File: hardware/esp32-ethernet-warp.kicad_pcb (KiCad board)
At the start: 4 copper layers, 104 x 42 mm, 117 parts, among them J201 TJLC_001LA1, P101 FLASH, P201 CON-SENSOR2, P202 CON-SENSOR2, P205 CON-SENSOR2, P206 CON-SENSOR2, Q101 BC817, Q102 BC817, SW101 B3U-1000P, SW102 B3U-1000P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

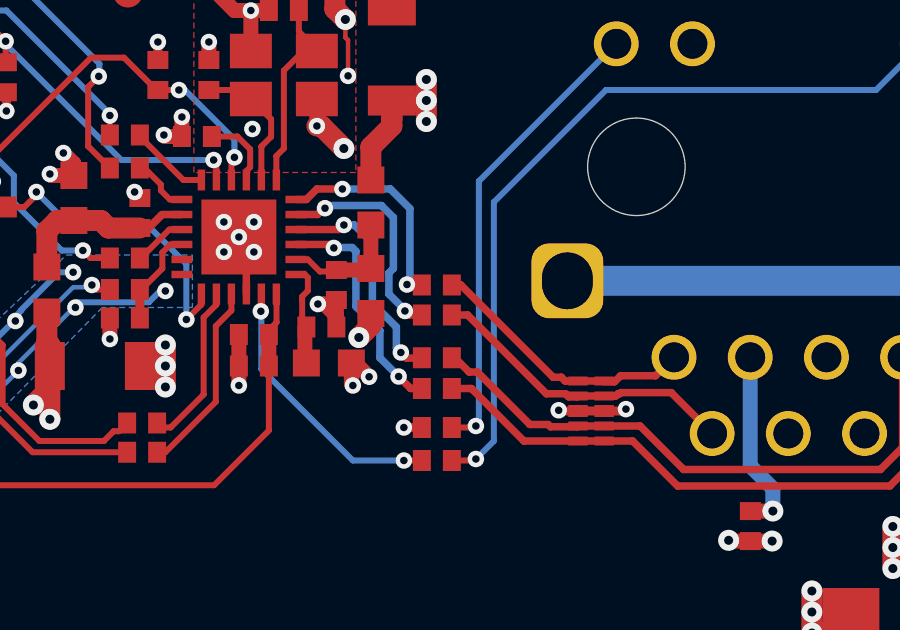
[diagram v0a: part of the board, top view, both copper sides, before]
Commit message: Revert "fix ethernet bug"
This reverts commit b0ba0365b1ecd3ee5b273f32dcba04a8b2befd97.
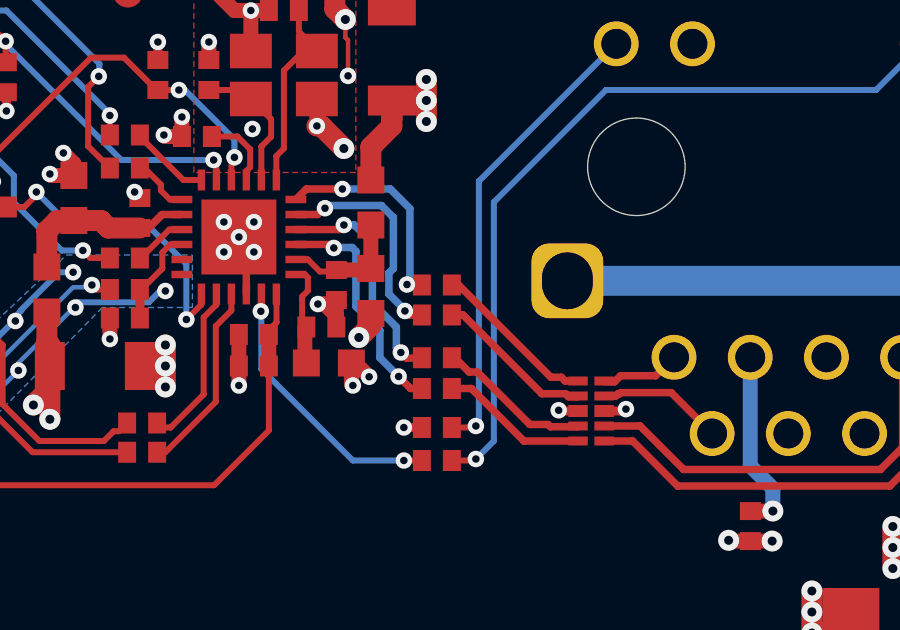
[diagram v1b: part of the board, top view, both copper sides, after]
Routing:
- net TXOPx: track 9.20 -> 8.22 mm
- net RXIPx: track 19.9 -> 19.0 mm
- net TXONx: track 10.4 -> 9.53 mm
- net RXINx: track 18.8 -> 17.9 mm
- net GND: track 266.9 -> 266.1 mm
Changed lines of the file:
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@@
   (segment (start 173.675 54.1) (end 174.375 54.1) (width 0.7) (layer "F.Cu") (net 1))
   (segment (start 201.45 26.635) (end 202.15 26.635) (width 0.5) (layer "F.Cu") (net 1))
-  (segment (start 240.755 32.25) (end 241.6 32.25) (width 0.3) (layer "F.Cu") (net 1))
   (segment (start 183.2233 40.7267) (end 183.225 40.725) (width 0.3) (layer "F.Cu") (net 1))
   (segment (start 229.85018 20.2499) (end 229.85018 18.90018) (width 0.5) (layer "F.Cu") (net 1))
@@
   (segment (start 221.675 20.025) (end 221.675 19.925) (width 0.2) (layer "B.Cu") (net 85))
   (segment (start 225.534166 23.884166) (end 221.675 20.025) (width 0.2) (layer "B.Cu") (net 85))
-  (segment (start 232.05 24.85) (end 232.9 24.85) (width 0.25) (layer "F.Cu") (net 86))
-  (segment (start 231.34992 25.20032) (end 231.69968 25.20032) (width 0.25) (layer "F.Cu") (net 86))
-  (segment (start 231.69968 25.20032) (end 232.05 24.85) (width 0.25) (layer "F.Cu") (net 86))
+  (segment (start 231.34992 25.20032) (end 231.70024 24.85) (width 0.25) (layer "F.Cu") (net 86))
+  (segment (start 231.70024 24.85) (end 232.9 24.85) (width 0.25) (layer "F.Cu") (net 86))
   (segment (start 235.069239 28.05) (end 235.053503 28.034264) (width 0.25) (layer "F.Cu") (net 86))
   (segment (start 235.55 28.05) (end 235.069239 28.05) (width 0.25) (layer "F.Cu") (net 86))
@@
   (segment (start 169.325 49.05) (end 167.725 49.05) (width 0.5) (layer "F.Cu") (net 138))
   (segment (start 168.025 49.15) (end 167.725 49.15) (width 0.2) (layer "F.Cu") (net 138))
-  (segment (start 236.85 28.05) (end 236.55 28.05) (width 0.25) (layer "F.Cu") (net 139))
-  (segment (start 239.925 31.125) (end 236.85 28.05) (width 0.25) (layer "F.Cu") (net 139))
+  (segment (start 239.85 31.125) (end 236.775 28.05) (width 0.25) (layer "F.Cu") (net 139))
   (segment (start 240.325 31.25) (end 240.2 31.125) (width 0.25) (layer "F.Cu") (net 139))
-  (segment (start 240.2 31.125) (end 239.925 31.125) (width 0.25) (layer "F.Cu") (net 139))
-  (segment (start 241.625 31.25) (end 240.65 31.25) (width 0.25) (layer "F.Cu") (net 139))
+  (segment (start 240.2 31.125) (end 239.85 31.125) (width 0.25) (layer "F.Cu") (net 139))
+  (segment (start 236.775 28.05) (end 236.55 28.05) (width 0.25) (layer "F.Cu") (net 139))
   (segment (start 243.34 31.075) (end 243.955 30.46) (width 0.25) (layer "F.Cu") (net 139))
   (segment (start 240.755 31.25) (end 240.325 31.25) (width 0.25) (layer "F.Cu") (net 139))
@@
   (segment (start 241.6 31.275) (end 241.975 31.275) (width 0.25) (layer "F.Cu") (net 139))
   (segment (start 242.175 31.075) (end 243.34 31.075) (width 0.25) (layer "F.Cu") (net 139))
+  (segment (start 240.755 31.75) (end 240.73 31.775) (width 0.25) (layer "F.Cu") (net 140))
+  (segment (start 236.925 29.05) (end 236.55 29.05) (width 0.25) (layer "F.Cu") (net 140))
   (segment (start 242.08608 31.675) (end 242.01108 31.75) (width 0.25) (layer "F.Cu") (net 140))
+  (segment (start 245.225 33) (end 243.862423 31.637423) (width 0.25) (layer "F.Cu") (net 140))
+  (segment (start 243.862423 31.637423) (end 242.178263 31.637423) (width 0.25) (layer "F.Cu") (net 140))
+  (segment (start 240.73 31.775) (end 240.437534 31.775) (width 0.25) (layer "F.Cu") (net 140))
   (segment (start 240.437534 31.775) (end 240.337534 31.675) (width 0.25) (layer "F.Cu") (net 140))
-  (segment (start 245.225 33) (end 243.862423 31.637423) (width 0.25) (layer "F.Cu") (net 140))
-  (segment (start 240.337534 31.675) (end 239.7 31.675) (width 0.25) (layer "F.Cu") (net 140))
-  (segment (start 243.862423 31.637423) (end 242.178263 31.637423) (width 0.25) (layer "F.Cu") (net 140))
-  (segment (start 239.7 31.675) (end 237.075 29.05) (width 0.25) (layer "F.Cu") (net 140))
   (segment (start 242.01108 31.75) (end 241.65 31.75) (width 0.25) (layer "F.Cu") (net 140))
-  (segment (start 240.73 31.775) (end 240.437534 31.775) (width 0.25) (layer "F.Cu") (net 140))
-  (segment (start 241.625 31.75) (end 240.75 31.75) (width 0.25) (layer "F.Cu") (net 140))
-  (segment (start 240.755 31.75) (end 240.73 31.775) (width 0.25) (layer "F.Cu") (net 140))
   (segment (start 242.178263 31.637423) (end 242.140685 31.675) (width 0.25) (layer "F.Cu") (net 140))
   (segment (start 242.140685 31.675) (end 242.08608 31.675) (width 0.25) (layer "F.Cu") (net 140))
-  (segment (start 237.075 29.05) (end 236.55 29.05) (width 0.25) (layer "F.Cu") (net 140))
-  (segment (start 239.832398 32.7755) (end 239.756898 32.7) (width 0.25) (layer "F.Cu") (net 141))
+  (segment (start 240.337534 31.675) (end 239.55 31.675) (width 0.25) (layer "F.Cu") (net 140))
+  (segment (start 239.55 31.675) (end 236.925 29.05) (width 0.25) (layer "F.Cu") (net 140))
   (segment (start 241.625 32.75) (end 242.825 32.75) (width 0.25) (layer "F.Cu") (net 141))
   (segment (start 240.7295 32.7755) (end 239.832398 32.7755) (width 0.25) (layer "F.Cu") (net 141))
   (segment (start 237.4 30.95) (end 237.125 30.95) (width 0.25) (layer "F.Cu") (net 141))
+  (segment (start 237.125 30.95) (end 236.675 30.5) (width 0.25) (layer "F.Cu") (net 141))
   (segment (start 242.825 32.75) (end 244.275 34.2) (width 0.25) (layer "F.Cu") (net 141))
   (segment (start 236.675 30.5) (end 236.55 30.5) (width 0.25) (layer "F.Cu") (net 141))
+  (segment (start 251.575 33.46) (end 251.575 30.46) (width 0.25) (layer "F.Cu") (net 141))
+  (segment (start 250.835 34.2) (end 251.575 33.46) (width 0.25) (layer "F.Cu") (net 141))
+  (segment (start 244.275 34.2) (end 250.835 34.2) (width 0.25) (layer "F.Cu") (net 141))
+  (segment (start 239.15 32.7) (end 237.4 30.95) (width 0.25) (layer "F.Cu") (net 141))
+  (segment (start 239.756898 32.7) (end 239.15 32.7) (width 0.25) (layer "F.Cu") (net 141))
   (segment (start 240.755 32.75) (end 240.7295 32.7755) (width 0.25) (layer "F.Cu") (net 141))
-  (segment (start 241.625 32.75) (end 240.7 32.75) (width 0.25) (layer "F.Cu") (net 141))
-  (segment (start 251.575 33.46) (end 251.575 30.46) (width 0.25) (layer "F.Cu") (net 141))
-  (segment (start 237.125 30.95) (end 236.675 30.5) (width 0.25) (layer "F.Cu") (net 141))
-  (segment (start 250.835 34.2) (end 251.575 33.46) (width 0.25) (layer "F.Cu") (net 141))
-  (segment (start 239.15 32.7) (end 237.4 30.95) (width 0.25) (layer "F.Cu") (net 141))
-  (segment (start 244.275 34.2) (end 250.835 34.2) (width 0.25) (layer "F.Cu") (net 141))
-  (segment (start 239.756898 32.7) (end 239.15 32.7) (width 0.25) (layer "F.Cu") (net 141))
-  (segment (start 241.625 33.25) (end 240.75 33.25) (width 0.25) (layer "F.Cu") (net 142))
+  (segment (start 239.832398 32.7755) (end 239.756898 32.7) (width 0.25) (layer "F.Cu") (net 141))
   (segment (start 241.625 33.25) (end 242.575 33.25) (width 0.25) (layer "F.Cu") (net 142))
   (segment (start 252.6 33.85) (end 252.85 33.6) (width 0.25) (layer "F.Cu") (net 142))

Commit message: fix ethernet bug
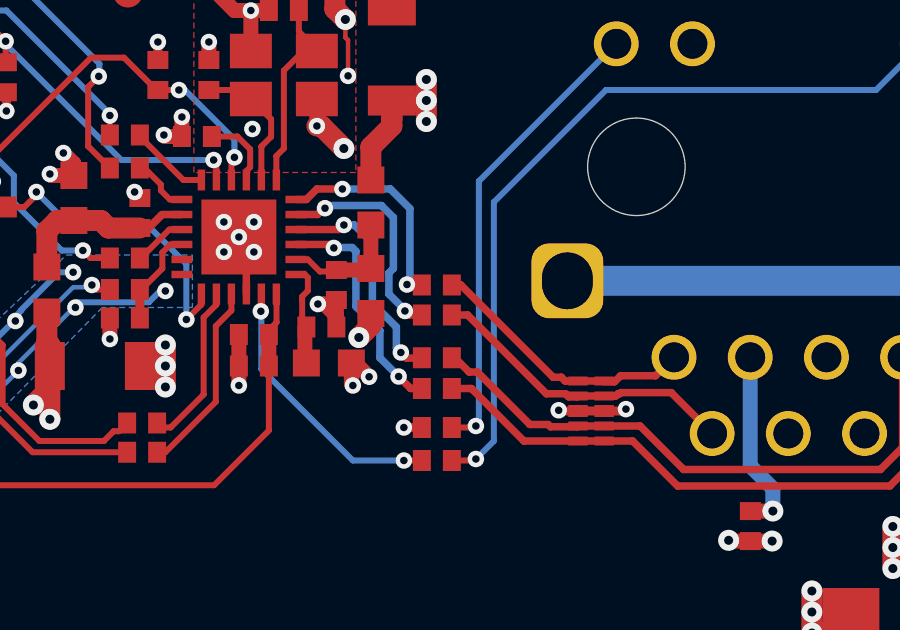
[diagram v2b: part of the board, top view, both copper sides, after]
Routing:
- net TXOPx: track 8.22 -> 9.20 mm
- net RXIPx: track 19.0 -> 19.9 mm
- net TXONx: track 9.53 -> 10.4 mm
- net RXINx: track 17.9 -> 18.8 mm
- net GND: track 266.1 -> 266.9 mm
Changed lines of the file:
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@@
   (segment (start 173.675 54.1) (end 174.375 54.1) (width 0.7) (layer "F.Cu") (net 1))
   (segment (start 201.45 26.635) (end 202.15 26.635) (width 0.5) (layer "F.Cu") (net 1))
+  (segment (start 240.755 32.25) (end 241.6 32.25) (width 0.3) (layer "F.Cu") (net 1))
   (segment (start 183.2233 40.7267) (end 183.225 40.725) (width 0.3) (layer "F.Cu") (net 1))
   (segment (start 229.85018 20.2499) (end 229.85018 18.90018) (width 0.5) (layer "F.Cu") (net 1))
@@
   (segment (start 221.675 20.025) (end 221.675 19.925) (width 0.2) (layer "B.Cu") (net 85))
   (segment (start 225.534166 23.884166) (end 221.675 20.025) (width 0.2) (layer "B.Cu") (net 85))
-  (segment (start 231.34992 25.20032) (end 231.70024 24.85) (width 0.25) (layer "F.Cu") (net 86))
-  (segment (start 231.70024 24.85) (end 232.9 24.85) (width 0.25) (layer "F.Cu") (net 86))
+  (segment (start 232.05 24.85) (end 232.9 24.85) (width 0.25) (layer "F.Cu") (net 86))
+  (segment (start 231.34992 25.20032) (end 231.69968 25.20032) (width 0.25) (layer "F.Cu") (net 86))
+  (segment (start 231.69968 25.20032) (end 232.05 24.85) (width 0.25) (layer "F.Cu") (net 86))
   (segment (start 235.069239 28.05) (end 235.053503 28.034264) (width 0.25) (layer "F.Cu") (net 86))
   (segment (start 235.55 28.05) (end 235.069239 28.05) (width 0.25) (layer "F.Cu") (net 86))
@@
   (segment (start 169.325 49.05) (end 167.725 49.05) (width 0.5) (layer "F.Cu") (net 138))
   (segment (start 168.025 49.15) (end 167.725 49.15) (width 0.2) (layer "F.Cu") (net 138))
-  (segment (start 239.85 31.125) (end 236.775 28.05) (width 0.25) (layer "F.Cu") (net 139))
+  (segment (start 236.85 28.05) (end 236.55 28.05) (width 0.25) (layer "F.Cu") (net 139))
+  (segment (start 239.925 31.125) (end 236.85 28.05) (width 0.25) (layer "F.Cu") (net 139))
   (segment (start 240.325 31.25) (end 240.2 31.125) (width 0.25) (layer "F.Cu") (net 139))
-  (segment (start 240.2 31.125) (end 239.85 31.125) (width 0.25) (layer "F.Cu") (net 139))
-  (segment (start 236.775 28.05) (end 236.55 28.05) (width 0.25) (layer "F.Cu") (net 139))
+  (segment (start 240.2 31.125) (end 239.925 31.125) (width 0.25) (layer "F.Cu") (net 139))
+  (segment (start 241.625 31.25) (end 240.65 31.25) (width 0.25) (layer "F.Cu") (net 139))
   (segment (start 243.34 31.075) (end 243.955 30.46) (width 0.25) (layer "F.Cu") (net 139))
   (segment (start 240.755 31.25) (end 240.325 31.25) (width 0.25) (layer "F.Cu") (net 139))
@@
   (segment (start 241.6 31.275) (end 241.975 31.275) (width 0.25) (layer "F.Cu") (net 139))
   (segment (start 242.175 31.075) (end 243.34 31.075) (width 0.25) (layer "F.Cu") (net 139))
+  (segment (start 242.08608 31.675) (end 242.01108 31.75) (width 0.25) (layer "F.Cu") (net 140))
+  (segment (start 240.437534 31.775) (end 240.337534 31.675) (width 0.25) (layer "F.Cu") (net 140))
+  (segment (start 245.225 33) (end 243.862423 31.637423) (width 0.25) (layer "F.Cu") (net 140))
+  (segment (start 240.337534 31.675) (end 239.7 31.675) (width 0.25) (layer "F.Cu") (net 140))
+  (segment (start 243.862423 31.637423) (end 242.178263 31.637423) (width 0.25) (layer "F.Cu") (net 140))
+  (segment (start 239.7 31.675) (end 237.075 29.05) (width 0.25) (layer "F.Cu") (net 140))
+  (segment (start 242.01108 31.75) (end 241.65 31.75) (width 0.25) (layer "F.Cu") (net 140))
+  (segment (start 240.73 31.775) (end 240.437534 31.775) (width 0.25) (layer "F.Cu") (net 140))
+  (segment (start 241.625 31.75) (end 240.75 31.75) (width 0.25) (layer "F.Cu") (net 140))
   (segment (start 240.755 31.75) (end 240.73 31.775) (width 0.25) (layer "F.Cu") (net 140))
-  (segment (start 236.925 29.05) (end 236.55 29.05) (width 0.25) (layer "F.Cu") (net 140))
-  (segment (start 242.08608 31.675) (end 242.01108 31.75) (width 0.25) (layer "F.Cu") (net 140))
-  (segment (start 245.225 33) (end 243.862423 31.637423) (width 0.25) (layer "F.Cu") (net 140))
-  (segment (start 243.862423 31.637423) (end 242.178263 31.637423) (width 0.25) (layer "F.Cu") (net 140))
-  (segment (start 240.73 31.775) (end 240.437534 31.775) (width 0.25) (layer "F.Cu") (net 140))
-  (segment (start 240.437534 31.775) (end 240.337534 31.675) (width 0.25) (layer "F.Cu") (net 140))
-  (segment (start 242.01108 31.75) (end 241.65 31.75) (width 0.25) (layer "F.Cu") (net 140))
   (segment (start 242.178263 31.637423) (end 242.140685 31.675) (width 0.25) (layer "F.Cu") (net 140))
   (segment (start 242.140685 31.675) (end 242.08608 31.675) (width 0.25) (layer "F.Cu") (net 140))
-  (segment (start 240.337534 31.675) (end 239.55 31.675) (width 0.25) (layer "F.Cu") (net 140))
-  (segment (start 239.55 31.675) (end 236.925 29.05) (width 0.25) (layer "F.Cu") (net 140))
+  (segment (start 237.075 29.05) (end 236.55 29.05) (width 0.25) (layer "F.Cu") (net 140))
+  (segment (start 239.832398 32.7755) (end 239.756898 32.7) (width 0.25) (layer "F.Cu") (net 141))
   (segment (start 241.625 32.75) (end 242.825 32.75) (width 0.25) (layer "F.Cu") (net 141))
   (segment (start 240.7295 32.7755) (end 239.832398 32.7755) (width 0.25) (layer "F.Cu") (net 141))
   (segment (start 237.4 30.95) (end 237.125 30.95) (width 0.25) (layer "F.Cu") (net 141))
-  (segment (start 237.125 30.95) (end 236.675 30.5) (width 0.25) (layer "F.Cu") (net 141))
   (segment (start 242.825 32.75) (end 244.275 34.2) (width 0.25) (layer "F.Cu") (net 141))
   (segment (start 236.675 30.5) (end 236.55 30.5) (width 0.25) (layer "F.Cu") (net 141))
+  (segment (start 240.755 32.75) (end 240.7295 32.7755) (width 0.25) (layer "F.Cu") (net 141))
+  (segment (start 241.625 32.75) (end 240.7 32.75) (width 0.25) (layer "F.Cu") (net 141))
   (segment (start 251.575 33.46) (end 251.575 30.46) (width 0.25) (layer "F.Cu") (net 141))
+  (segment (start 237.125 30.95) (end 236.675 30.5) (width 0.25) (layer "F.Cu") (net 141))
   (segment (start 250.835 34.2) (end 251.575 33.46) (width 0.25) (layer "F.Cu") (net 141))
+  (segment (start 239.15 32.7) (end 237.4 30.95) (width 0.25) (layer "F.Cu") (net 141))
   (segment (start 244.275 34.2) (end 250.835 34.2) (width 0.25) (layer "F.Cu") (net 141))
-  (segment (start 239.15 32.7) (end 237.4 30.95) (width 0.25) (layer "F.Cu") (net 141))
   (segment (start 239.756898 32.7) (end 239.15 32.7) (width 0.25) (layer "F.Cu") (net 141))
-  (segment (start 240.755 32.75) (end 240.7295 32.7755) (width 0.25) (layer "F.Cu") (net 141))
-  (segment (start 239.832398 32.7755) (end 239.756898 32.7) (width 0.25) (layer "F.Cu") (net 141))
+  (segment (start 241.625 33.25) (end 240.75 33.25) (width 0.25) (layer "F.Cu") (net 142))
   (segment (start 241.625 33.25) (end 242.575 33.25) (width 0.25) (layer "F.Cu") (net 142))
   (segment (start 252.6 33.85) (end 252.85 33.6) (width 0.25) (layer "F.Cu") (net 142))
